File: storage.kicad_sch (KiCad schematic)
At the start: 14 parts, among them J11 microSD, Molex 104031-0811 pu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, U24 W25Q64JVSSIQ, 64 Mbit QSPI NOR

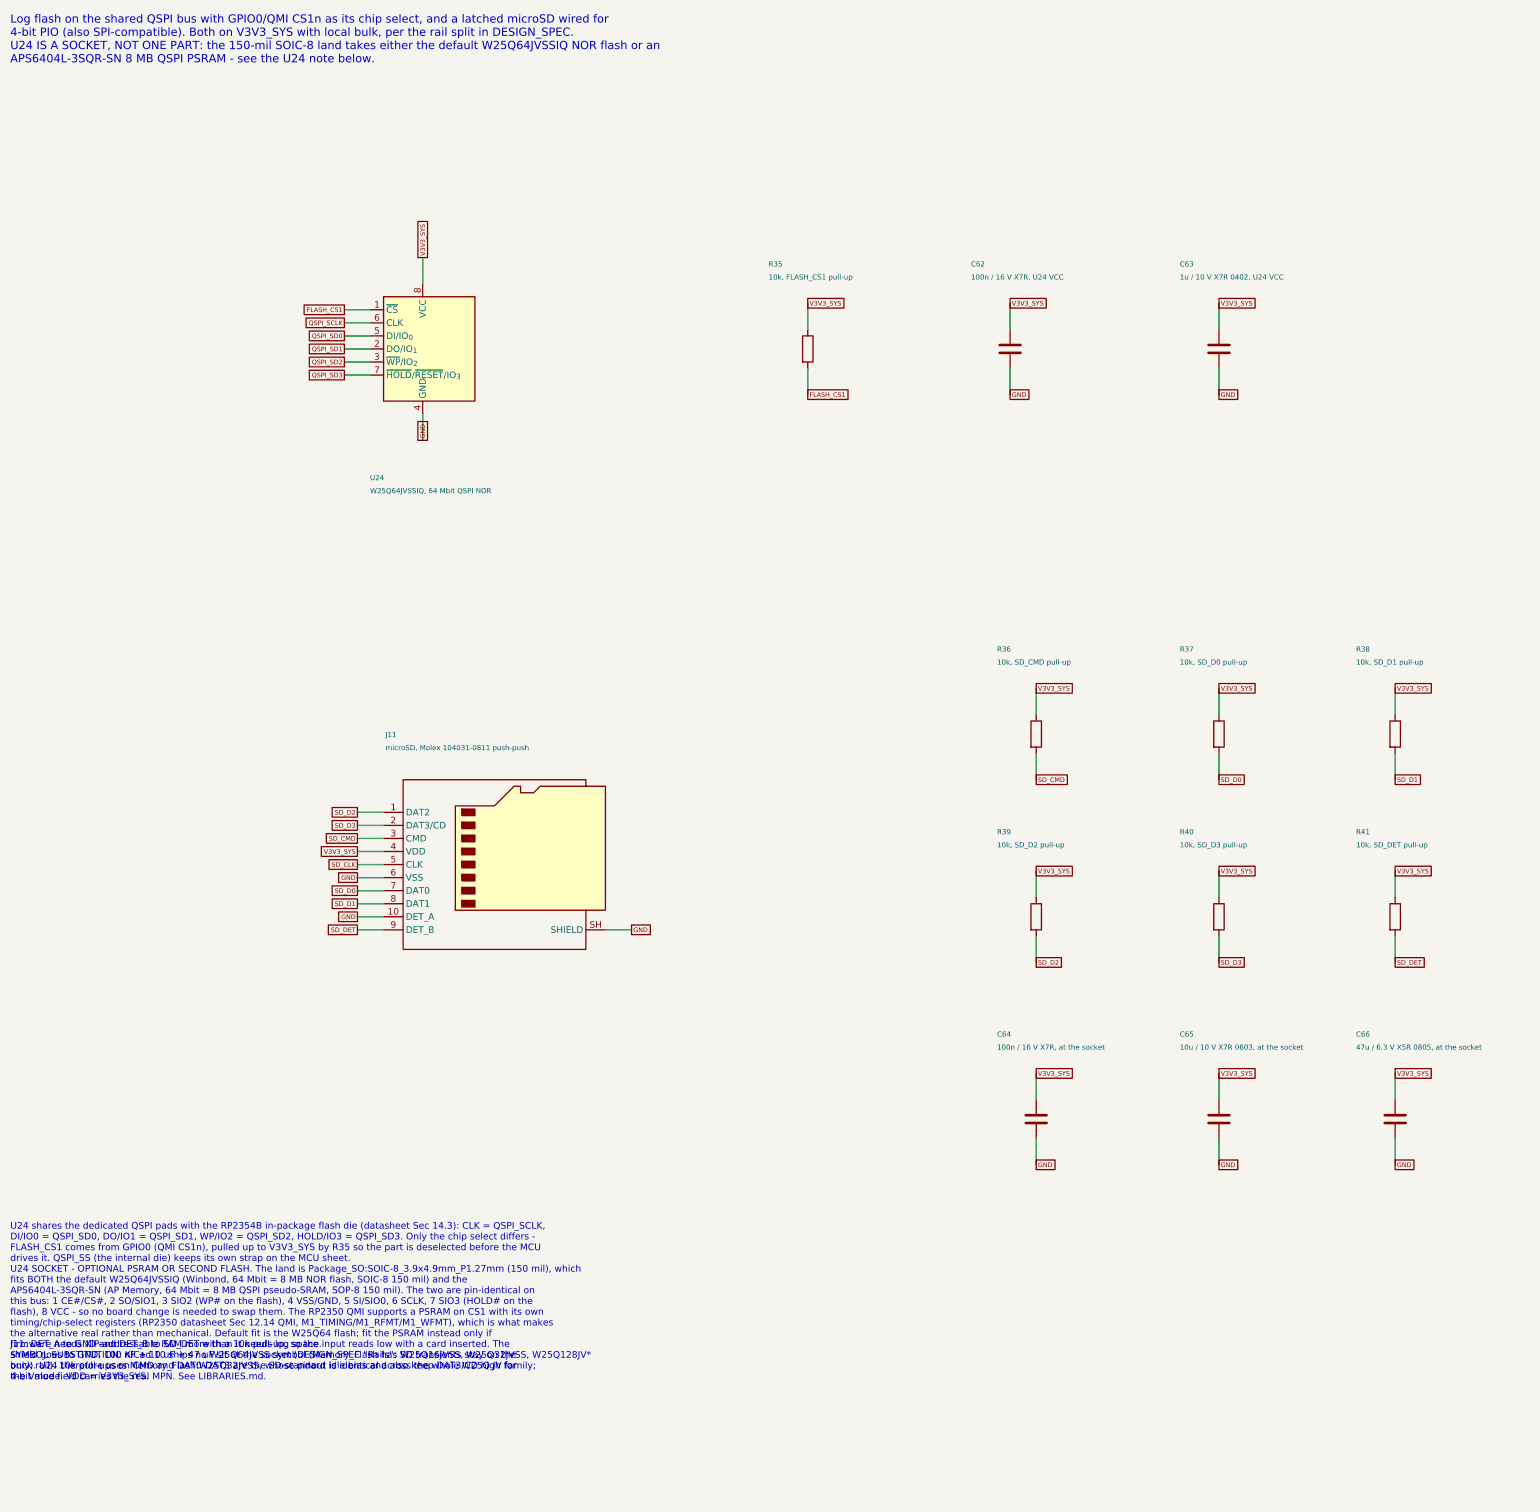
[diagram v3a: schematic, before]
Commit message: Flash socket becomes an optional back-side expansion; ESC row on the back edge; C19 100 uF
U24 (SOIC-8 150 mil) and its caps C62/C63 are DNP, excluded from the BOM
and placed flipped on the back with a legend ("FLASH / PSRAM EXPANSION,
SOIC-8 150mil, QMI CS1, W25Q64JVSSIQ or APS6404L-3SQR-SN"); the RP2354B's
internal 2 MB flash and the microSD cover firmware and logging. The ESC pad
row J3 sits along the left edge on the back, like the DBG row on the bottom
edge. C19 (V5_SYS bulk) reduced from 220 uF D-case to 100 uF 6.3 V B-case:
the ngspice decks now use CPOLY=100u and every handover predicate still
passes (worst-case V5_SYS min 4.37 V). Board 46.6 x 41.2 mm; DRC
unrouted-only; ERC 0/0, checker PASS, audit 140/140.

Co-Authored-By: Claude Fable 5.1 <noreply@anthropic.com>
Claude-Session: https://claude.ai/code/session_01U6Ud7JA3CDTJZVcZZr5sx1
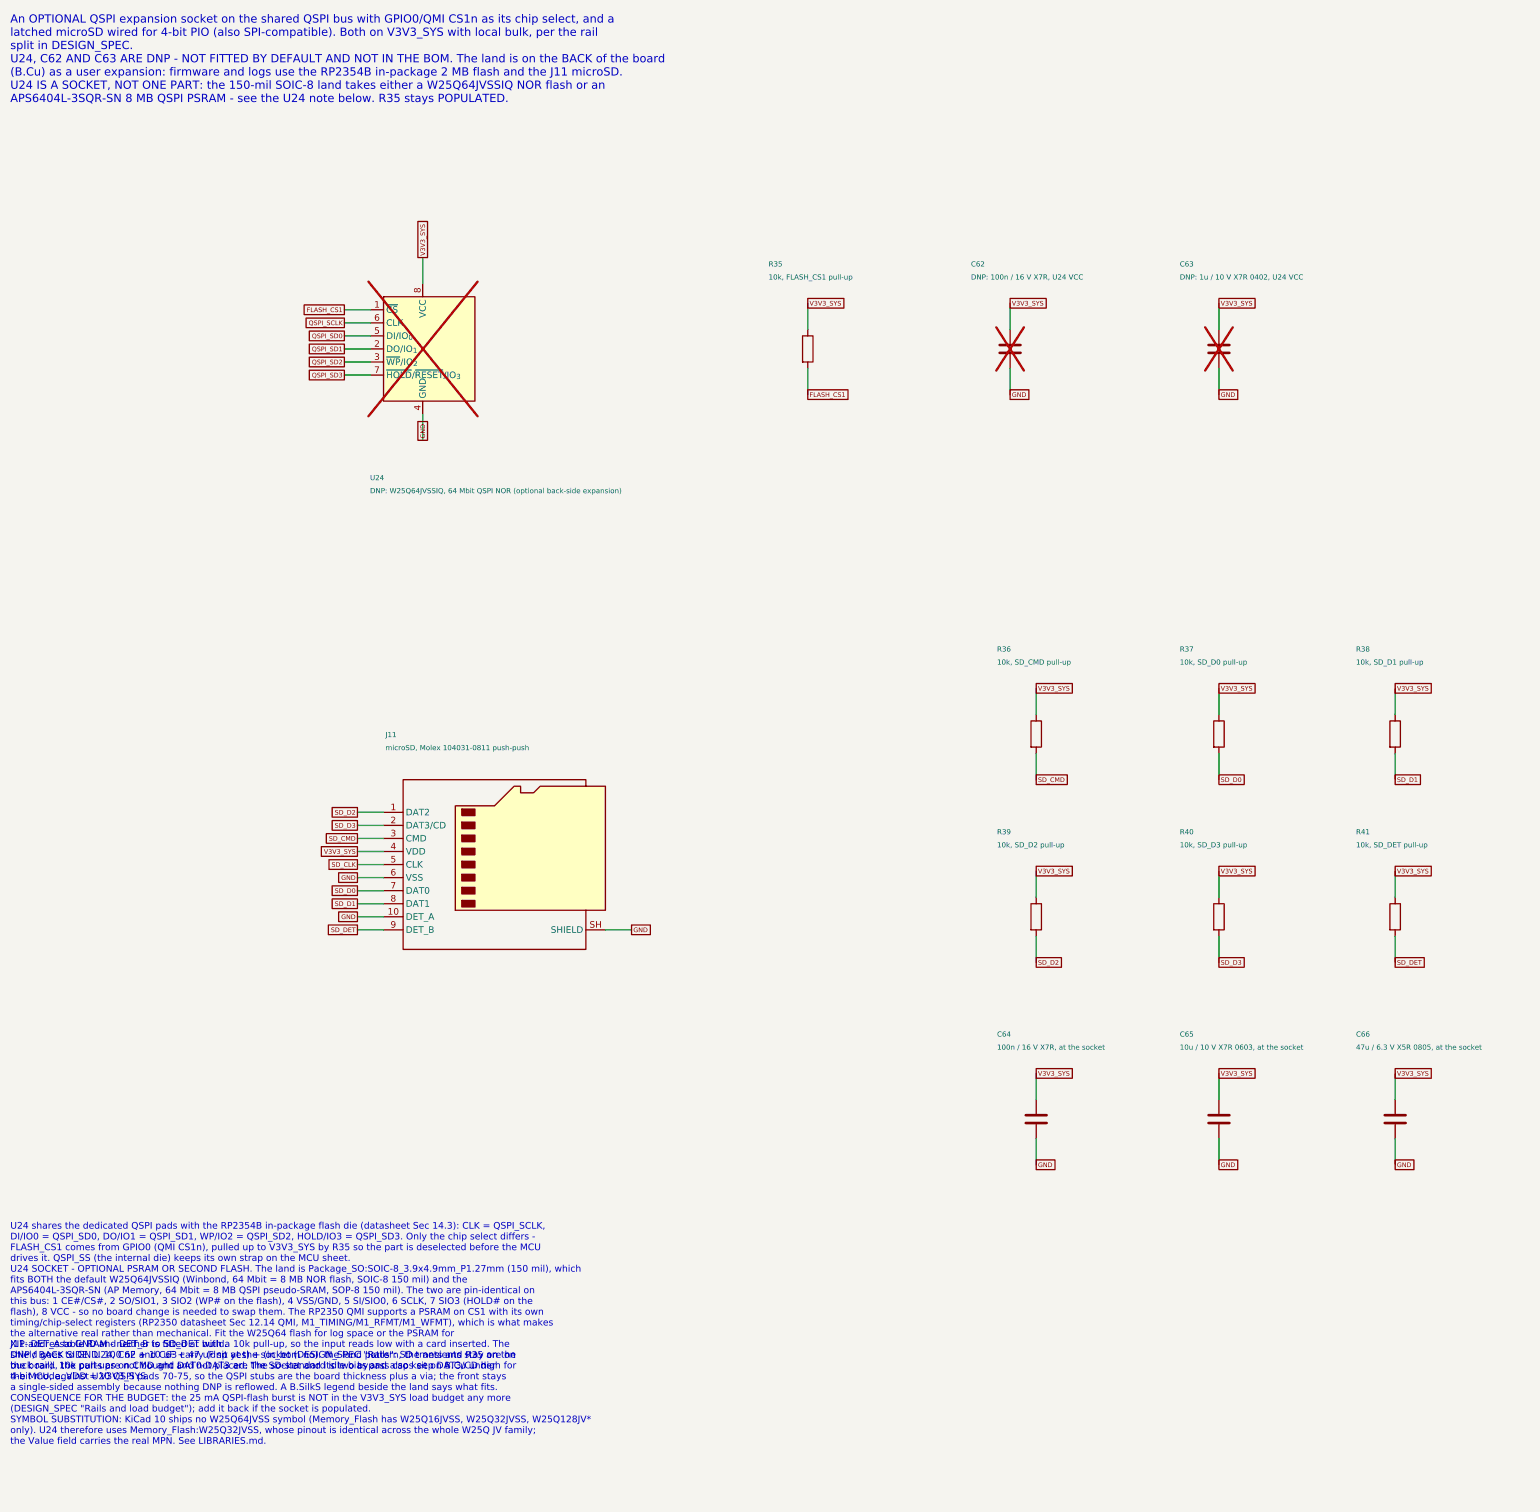
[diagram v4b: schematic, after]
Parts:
- C62: value 100n / 16 V X7R, U24 VCC -> DNP: 100n / 16 V X7R, U24 VCC; now not fitted; now left out of the parts list
- C63: value 1u / 10 V X7R 0402, U24 VCC -> DNP: 1u / 10 V X7R 0402, U24 VCC; now not fitted; now left out of the parts list
- U24: value W25Q64JVSSIQ, 64 Mbit QSPI NOR -> DNP: W25Q64JVSSIQ, 64 Mbit QSPI NOR (optional back-side expansion); now not fitted; now left out of the parts list
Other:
- note added: "An OPTIONAL QSPI expansion socket on the shared QSPI bus with GPIO0/QMI CS1n as its chip select, and a latched microSD wired for 4-bit PIO (also SPI-compatible). Both on V3V3_SYS with local bulk, per the rail split in DESIGN_SPEC. U24, C62 AND C63 ARE DNP - NOT FITTED BY DEFAULT AND NOT IN THE BOM. The land is on the BACK of the board (B.Cu) as a user expansion: firmware and logs use the RP2354B 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"
- note removed: "Log flash on the shared QSPI bus with GPIO0/QMI CS1n as its chip select, and a latched microSD wired for 4-bit PIO (also SPI-compatible). Both on V3V3_SYS with local bulk, per the rail split in DESIGN_SPEC. U24 IS A SOCKET, NOT ONE PART: the 150-mil SOIC-8 land takes either the default W25Q64JVSSIQ NOR flash or an APS6404L-3SQR-SN 8 MB QSPI PSRAM - see the U24 note below."

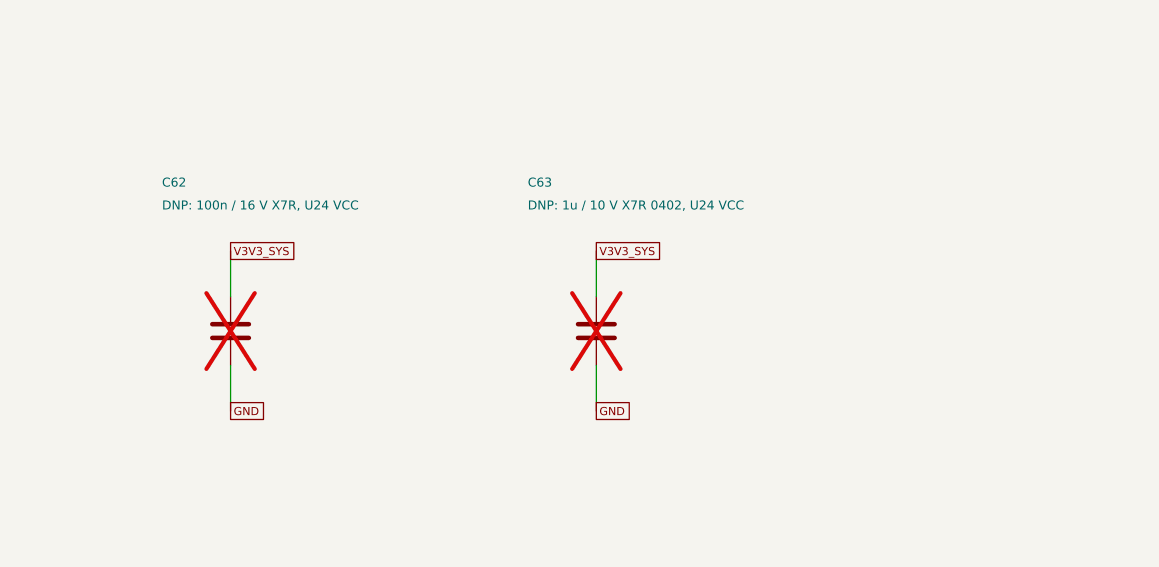
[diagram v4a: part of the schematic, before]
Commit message: Flash-socket caps back on the front, minimal socket silk; L2 to XGL3020-222
C62/C63 (U24 decoupling) are fitted on the front again, so a user adding a
flash or PSRAM chip to the back-side SOIC-8 socket only solders the chip;
the back legend is reduced to "FLASH" / "SOIC-8" plus the pin-1 mark, and
the compatible parts (150-mil SOIC-8 QSPI NOR: W25Q16/32/64JVSS, GD25Q32C/
64C, MX25L3233F/6433F; QSPI PSRAM: APS6404L-3SQR-SN, ESP-PSRAM64H, IPS6404L,
LY68L6400) are documented in DESIGN_SPEC/LIBRARIES.

L2 (TPS62913 3.3 V buck inductor) shrinks from XGL4030-222 (4x4x3.1) to
Coilcraft XGL3020-222MEC (3x3x2.0; Isat 2.2 A @20 %, 2.85 A @30 %, DCR
30.5 mOhm, Doc 1776 Rev 02/19/26) against a ~0.95 A peak; project footprint
from the Coilcraft land pattern, vendor STEP aligned and verified against
copper. L3 stays XGL4030-472: its floor is the AP63205's 3.1 A current-limit
ceiling and the XGL4020 shares the 4x4 land pattern. Board 46.6 x 41.2 mm;
DRC unrouted-only; ERC 0/0, checker PASS, ngspice PASS, audit 140/140.

Co-Authored-By: Claude Fable 5.1 <noreply@anthropic.com>
Claude-Session: https://claude.ai/code/session_01U6Ud7JA3CDTJZVcZZr5sx1
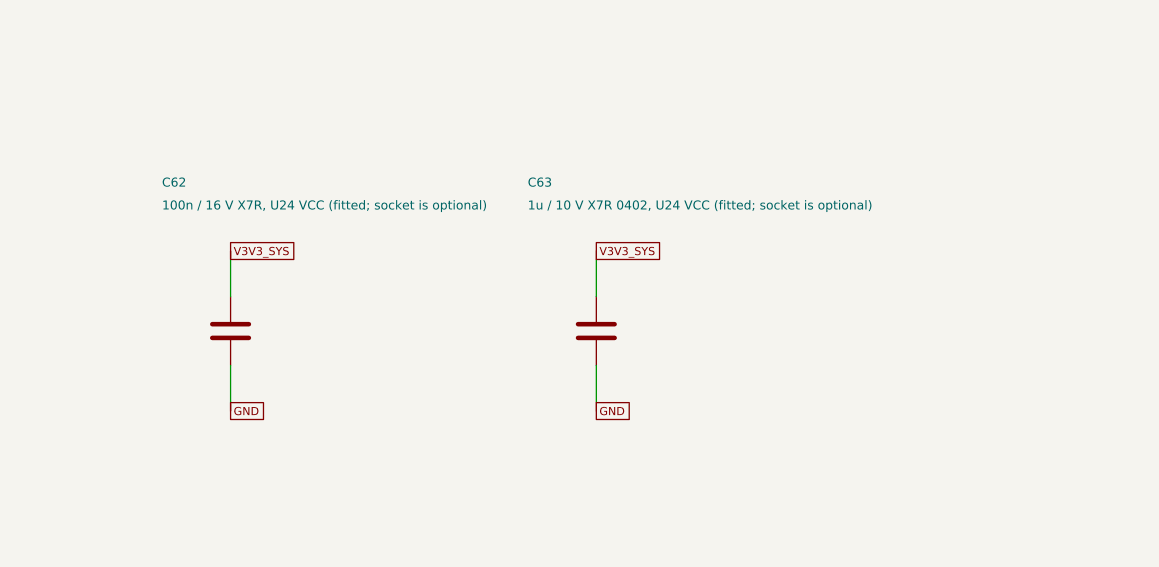
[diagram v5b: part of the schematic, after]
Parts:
- C62: value DNP: 100n / 16 V X7R, U24 VCC -> 100n / 16 V X7R, U24 VCC (fitted; socket is optional); now fitted; now in the parts list
- C63: value DNP: 1u / 10 V X7R 0402, U24 VCC -> 1u / 10 V X7R 0402, U24 VCC (fitted; socket is optional); now fitted; now in the parts list
